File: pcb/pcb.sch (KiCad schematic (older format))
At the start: 86 parts, among them J1 USB-Mini, J2 Conn_01x04, P1 i2c-pin1, P2 i2c-pin2, SW1 SW_Push, SW10 SW_Push, SW11 SW_Push, SW12 SW_Push, SW13 SW_Push, SW14 SW_Push, SW15 SW_Push, SW16 SW_Push, SW17 SW_Push, SW18 SW_Push, SW19 SW_Push, SW2 SW_Push, SW20 SW_Push, SW21 SW_Push, SW22 SW_Push, SW23 SW_Push, SW24 SW_Push, SW25 SW_Push, SW26 SW_Push, SW27 SW_Push, SW28 SW_Push, SW29 SW_Push, SW3 SW_Push, SW30 SW_Push, SW31 SW_Push, SW32 SW_Push, SW33 SW_Push, SW34 SW_Push, SW35 SW_Push, SW36 SW_Push, SW37 SW_Push, SW38 SW_Push, SW39 SW_Push, SW4 SW_Push, SW40 SW_Push, SW5 SW_Push, SW6 SW_Push, SW7 SW_Push, SW8 SW_Push, SW9 SW_Push, U1 ProMicro, U2 TRRS

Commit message: finished case and pcb prototype
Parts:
- J2: value Conn_01x04 -> Conn_01x05; footprint Connector_PinHeader_2.54mm:PinHeader_1x04_P2.54mm_Vertical -> Connector_PinHeader_2.54mm:PinHeader_1x05_P2.54mm_Vertical; symbol Connector_Generic:Conn_01x04 -> Connector_Generic:Conn_01x05
- RSW1: footprint Keebio-Parts:SW_Tactile_SPST_Angled_MJTP1117 -> kbd:ResetSW
- U1: footprint Keebio-Parts:ArduinoProMicro-ZigZag -> Keebio-Parts:ArduinoProMicro
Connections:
- net col6: now also U1.17 (A0/PF7); no longer U1.11 (8/PB4)
- net row0: now also U1.11 (8/PB4); no longer U1.16 (15/PB1)
- net row1: now also U1.19 (A2/PF5); no longer U1.15 (14/PB3)
- net row2: now also U1.18 (A1/PF6); no longer U1.14 (16/PB2)
- net at J1.4 (ID): now also J2.5 (Pin_5)
- no-connect marks 7 -> 6
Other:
- moved on the sheet: J1
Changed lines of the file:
@@
 L keebio:USB-Mini J1
 U 1 1 60852385
-P 1700 1900
-F 0 "J1" H 1683 2597 60  0000 C CNN
-F 1 "USB-Mini" H 1683 2491 60  0000 C CNN
-F 2 "Keebio-Parts:USB-Mini-B_2leg" H 1650 1950 60  0001 C CNN
-F 3 "" H 1650 1950 60  0001 C CNN
-	1    1700 1900
+P 1150 2100
+F 0 "J1" H 1133 2797 60  0000 C CNN
+F 1 "USB-Mini" H 1133 2691 60  0000 C CNN
+F 2 "Keebio-Parts:USB-Mini-B_2leg" H 1100 2150 60  0001 C CNN
+F 3 "" H 1100 2150 60  0001 C CNN
+	1    1150 2100
 	1    0    0    -1
 $EndComp
@@
 col5
 Text HLabel 8550 5000 0    50   Input ~ 0
-col6
-Text HLabel 9950 4800 2    50   Input ~ 0
 row0
-Text HLabel 9950 4900 2    50   Input ~ 0
+Text HLabel 9950 4500 2    50   Input ~ 0
 row1
-Text HLabel 9950 5000 2    50   Input ~ 0
+Text HLabel 9950 4600 2    50   Input ~ 0
 row2
-Text HLabel 9950 5100 2    50   Input ~ 0
-row3
 Text HLabel 8550 5100 0    50   Input ~ 0
 row4
@@
 F 0 "U1" H 9250 5387 60  0000 C CNN
 F 1 "ProMicro" H 9250 5281 60  0000 C CNN
-F 2 "Keebio-Parts:ArduinoProMicro-ZigZag" V 10300 2050 60  0001 C CNN
+F 2 "Keebio-Parts:ArduinoProMicro" V 10300 2050 60  0001 C CNN
 F 3 "" V 10300 2050 60  0001 C CNN
 	1    9250 4550
@@
 F 0 "RSW1" H 9250 3405 50  0000 C CNN
 F 1 "SW_PUSH" H 9250 3314 50  0000 C CNN
-F 2 "Keebio-Parts:SW_Tactile_SPST_Angled_MJTP1117" H 9250 3313 50  0001 C CNN
+F 2 "kbd:ResetSW" H 9250 3313 50  0001 C CNN
 F 3 "" H 9250 3150 50  0000 C CNN
 	1    9250 3150
@@
 data
 $Comp
-L Connector_Generic:Conn_01x04 J2
+L Connector_Generic:Conn_01x05 J2
 U 1 1 60A9C567
-P 2900 1500
-F 0 "J2" H 2980 1492 50  0000 L CNN
-F 1 "Conn_01x04" H 2980 1401 50  0000 L CNN
-F 2 "Connector_PinHeader_2.54mm:PinHeader_1x04_P2.54mm_Vertical" H 2900 1500 50  0001 C CNN
-F 3 "~" H 2900 1500 50  0001 C CNN
-	1    2900 1500
-	1    0    0    -1
-$EndComp
-Wire Wire Line
-	2300 1850 1900 1850
-NoConn ~ 1900 1750
+P 1900 1750
+F 0 "J2" H 1980 1742 50  0000 L CNN
+F 1 "Conn_01x05" H 1980 1651 50  0000 L CNN
+F 2 "Connector_PinHeader_2.54mm:PinHeader_1x05_P2.54mm_Vertical" H 1900 1750 50  0001 C CNN
+F 3 "~" H 1900 1750 50  0001 C CNN
+	1    1900 1750
+	1    0    0    -1
+$EndComp
 NoConn ~ 8550 4000
 NoConn ~ 9950 4400
-NoConn ~ 9950 4500
-NoConn ~ 9950 4600
-NoConn ~ 9950 4700
+NoConn ~ 9950 5000
+NoConn ~ 9950 4900
 NoConn ~ 9950 4000
 $Comp
@@
 Connection ~ 6000 4400
 Wire Wire Line
-	1900 1450 2650 1450
-Wire Wire Line
-	2650 1450 2650 1500
-Wire Wire Line
-	2650 1500 2700 1500
-Wire Wire Line
-	2300 1700 2700 1700
-Wire Wire Line
-	2300 1700 2300 1850
-Wire Wire Line
-	1900 1650 2400 1650
-Wire Wire Line
-	2400 1650 2400 1600
-Wire Wire Line
-	2400 1600 2700 1600
-Wire Wire Line
-	2350 1550 2350 1400
-Wire Wire Line
-	2350 1400 2700 1400
-Wire Wire Line
-	1900 1550 2350 1550
-Wire Wire Line
 	2250 4200 2250 4050
 Wire Wire Line
@@
 	1150 6150 2250 6150
 Connection ~ 2250 6000
+Wire Wire Line
+	1350 1650 1700 1650
+Wire Wire Line
+	1700 1950 1350 1950
+Wire Wire Line
+	1350 1750 1400 1750
+Wire Wire Line
+	1400 1750 1400 1550
+Wire Wire Line
+	1400 1550 1700 1550
+Wire Wire Line
+	1350 1850 1500 1850
+Wire Wire Line
+	1500 1850 1500 1750
+Wire Wire Line
+	1500 1750 1700 1750
+Wire Wire Line
+	1350 2050 1600 2050
+Wire Wire Line
+	1600 2050 1600 1850
+Wire Wire Line
+	1600 1850 1700 1850
+Text HLabel 9950 4700 2    50   Input ~ 0
+col6
+Text HLabel 9950 5100 2    50   Input ~ 0
+row3
+NoConn ~ 9950 4800
 $EndSCHEMATC

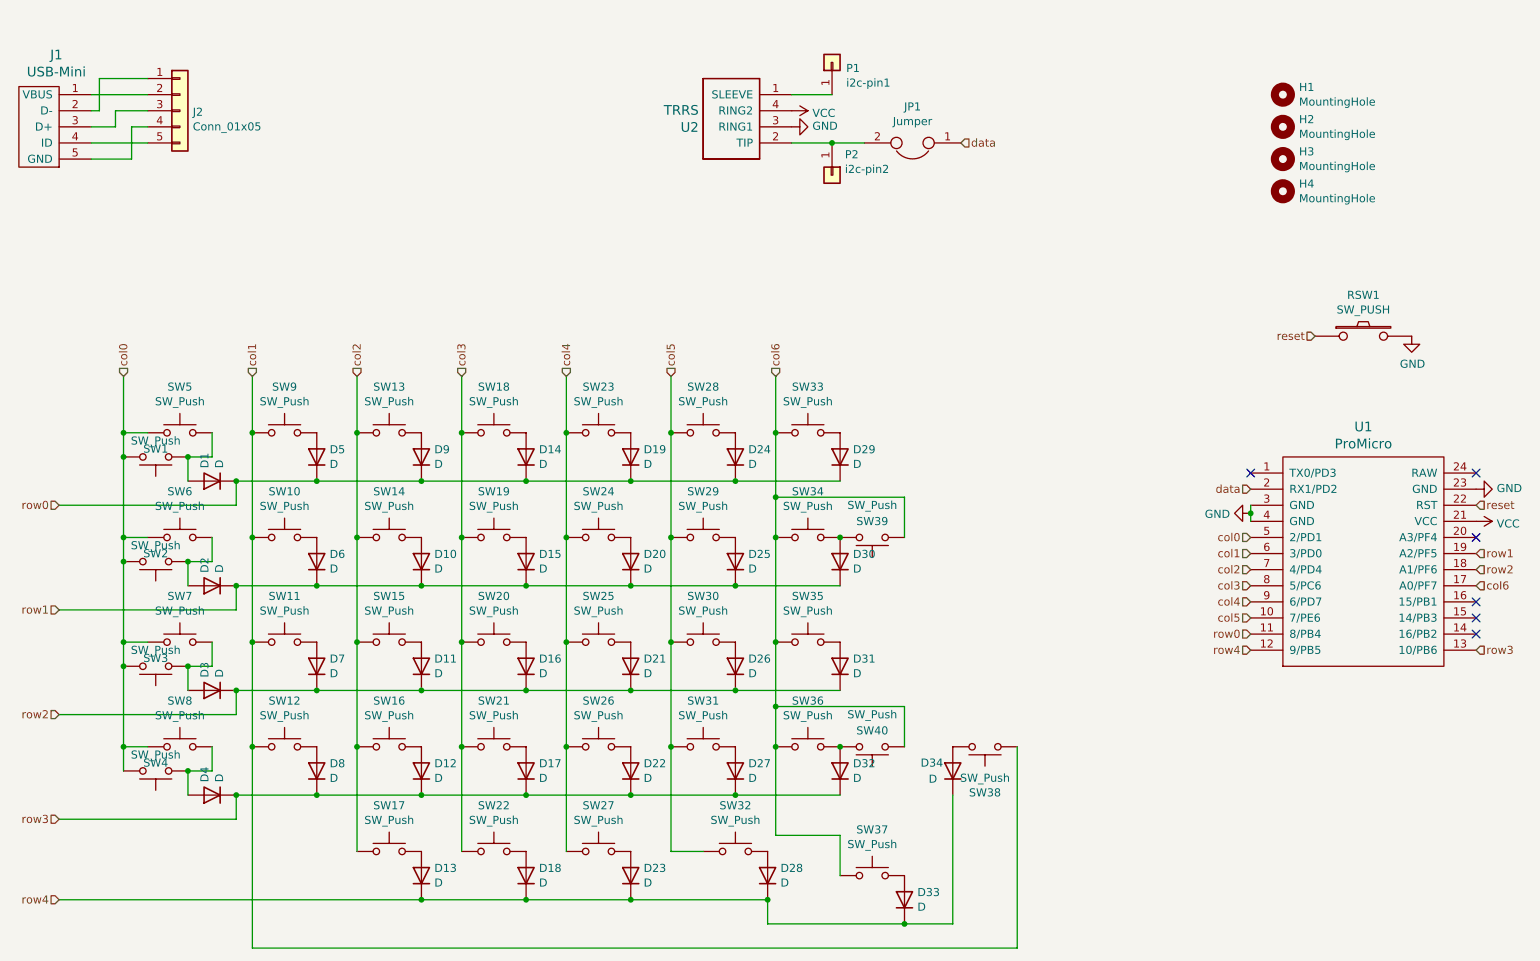
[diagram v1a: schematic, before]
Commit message: finalised pcb rev1.1
added support for an encoder
added support for a stablized 2u key on the double thumb keys
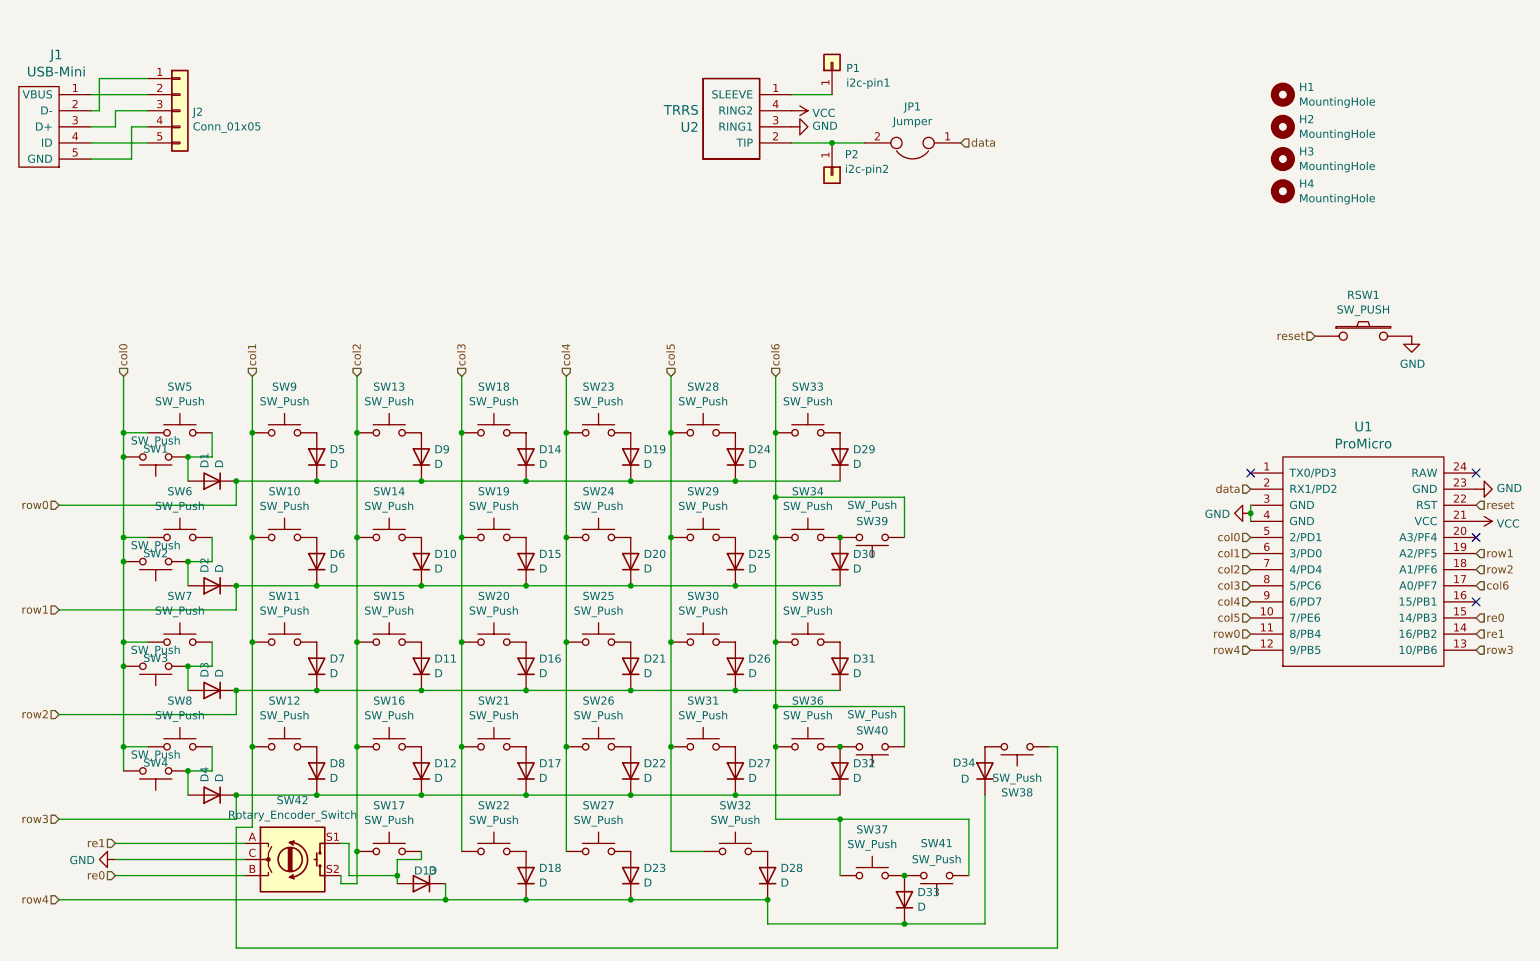
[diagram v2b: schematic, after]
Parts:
- added SW41: SW_Push, keyswitches:SW_MX_reversible, symbol Switch:SW_Push
- added SW42: Rotary_Encoder_Switch, local:RotaryEncoder_Alps_EC11E-Switch_Vertical_H20mm, symbol Device:Rotary_Encoder_Switch
- H1, H2, H3, H4: footprint local:m4.5_hole -> local:m2.4_hole_plated
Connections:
- net GND: now also SW42.C
- net col2: now also SW42.S2
- net col6: now also SW41.1
- net re1: now reaches U1.14 (16/PB2)
- net re1: now also SW42.A
- net re0: now reaches U1.15 (14/PB3)
- net re0: now also SW42.B
- net at D13.2 (A), SW17.2: now also SW42.S1
- net at D33.2 (A), SW37.2: now also SW41.2
- no-connect marks 6 -> 4
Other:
- moved on the sheet: D13, D34, SW38
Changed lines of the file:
@@
 L Device:D D13
 U 1 1 609271B4
-P 3400 6500
-F 0 "D13" V 3446 6420 50  0000 R CNN
-F 1 "D" V 3355 6420 50  0000 R CNN
-F 2 "Keebio-Parts:Diode-dual" H 3400 6500 50  0001 C CNN
-F 3 "~" H 3400 6500 50  0001 C CNN
-	1    3400 6500
-	0    -1   -1   0
+P 3400 6550
+F 0 "D13" H 3446 6470 50  0000 R CNN
+F 1 "D" H 3355 6470 50  0000 R CNN
+F 2 "Keebio-Parts:Diode-dual" H 3400 6550 50  0001 C CNN
+F 3 "~" H 3400 6550 50  0001 C CNN
+	1    3400 6550
+	-1   0    0    1
 $EndComp
 $Comp
@@
 	0    -1   -1   0
 $EndComp
-Wire Wire Line
-	3400 6650 4050 6650
 $Comp
 L Switch:SW_Push SW27
@@
 L Switch:SW_Push SW38
 U 1 1 6092E91E
-P 6900 5700
-F 0 "SW38" H 6900 5985 50  0000 C CNN
-F 1 "SW_Push" H 6900 5894 50  0000 C CNN
-F 2 "keyswitches:SW_MX_reversible" H 6900 5900 50  0001 C CNN
-F 3 "~" H 6900 5900 50  0001 C CNN
-	1    6900 5700
+P 7100 5700
+F 0 "SW38" H 7100 5985 50  0000 C CNN
+F 1 "SW_Push" H 7100 5894 50  0000 C CNN
+F 2 "keyswitches:SW_MX_reversible" H 7100 5900 50  0001 C CNN
+F 3 "~" H 7100 5900 50  0001 C CNN
+	1    7100 5700
 	-1   0    0    1
 $EndComp
@@
 L Device:D D34
 U 1 1 6092E924
-P 6700 5850
-F 0 "D34" V 6750 6050 50  0000 R CNN
-F 1 "D" V 6650 6000 50  0000 R CNN
-F 2 "Keebio-Parts:Diode-dual" H 6700 5850 50  0001 C CNN
-F 3 "~" H 6700 5850 50  0001 C CNN
-	1    6700 5850
+P 6900 5850
+F 0 "D34" V 6950 6050 50  0000 R CNN
+F 1 "D" V 6850 6000 50  0000 R CNN
+F 2 "Keebio-Parts:Diode-dual" H 6900 5850 50  0001 C CNN
+F 3 "~" H 6900 5850 50  0001 C CNN
+	1    6900 5850
 	0    -1   -1   0
 $EndComp
@@
 Connection ~ 4700 6650
 Connection ~ 4050 6650
-Connection ~ 3400 6650
 Wire Wire Line
 	5550 6650 5550 6800
@@
 Wire Wire Line
 	4950 6350 5150 6350
-Wire Wire Line
-	5600 6250 6000 6250
-Wire Wire Line
-	6000 6250 6000 6500
 $Comp
 L Device:D D5
@@
 Connection ~ 4050 4050
 Wire Wire Line
-	5600 5700 5600 6250
+	5600 5700 5600 6150
 Connection ~ 5600 5700
 Wire Wire Line
@@
 	3650 5700 3650 6350
 Connection ~ 3650 5700
-Wire Wire Line
-	3000 6350 3000 5700
 Connection ~ 3000 5700
 Wire Wire Line
-	2350 5700 2350 6950
+	2350 5700 2350 6200
 Connection ~ 2350 5700
-Wire Wire Line
-	6700 6000 6700 6800
-Wire Wire Line
-	6700 6800 6400 6800
 Connection ~ 6400 6800
-Wire Wire Line
-	7100 6950 7100 5700
-Wire Wire Line
-	2350 6950 7100 6950
 $Comp
 L Switch:SW_Push SW1
@@
 Wire Wire Line
 	1550 3400 1550 3750
-Wire Wire Line
-	1150 6650 3400 6650
 Wire Wire Line
 	1700 5050 1550 5050
@@
 NoConn ~ 8550 4000
 NoConn ~ 9950 4400
-NoConn ~ 9950 5000
-NoConn ~ 9950 4900
 NoConn ~ 9950 4000
 $Comp
@@
 F 0 "H1" H 8850 1696 50  0000 L CNN
 F 1 "MountingHole" H 8850 1605 50  0000 L CNN
-F 2 "local:m4.5_hole" H 8750 1650 50  0001 C CNN
+F 2 "local:m2.4_hole_plated" H 8750 1650 50  0001 C CNN
 F 3 "~" H 8750 1650 50  0001 C CNN
 	1    8750 1650
@@
 F 0 "H2" H 8850 1896 50  0000 L CNN
 F 1 "MountingHole" H 8850 1805 50  0000 L CNN
-F 2 "local:m4.5_hole" H 8750 1850 50  0001 C CNN
+F 2 "local:m2.4_hole_plated" H 8750 1850 50  0001 C CNN
 F 3 "~" H 8750 1850 50  0001 C CNN
 	1    8750 1850
@@
 F 0 "H3" H 8850 2096 50  0000 L CNN
 F 1 "MountingHole" H 8850 2005 50  0000 L CNN
-F 2 "local:m4.5_hole" H 8750 2050 50  0001 C CNN
+F 2 "local:m2.4_hole_plated" H 8750 2050 50  0001 C CNN
 F 3 "~" H 8750 2050 50  0001 C CNN
 	1    8750 2050
@@
 F 0 "H4" H 8850 2296 50  0000 L CNN
 F 1 "MountingHole" H 8850 2205 50  0000 L CNN
-F 2 "local:m4.5_hole" H 8750 2250 50  0001 C CNN
+F 2 "local:m2.4_hole_plated" H 8750 2250 50  0001 C CNN
 F 3 "~" H 8750 2250 50  0001 C CNN
 	1    8750 2250
@@
 row3
 NoConn ~ 9950 4800
+$Comp
+L Switch:SW_Push SW41
+U 1 1 609871D1
+P 6600 6500
+F 0 "SW41" H 6600 6300 50  0000 C CNN
+F 1 "SW_Push" H 6600 6400 50  0000 C CNN
+F 2 "keyswitches:SW_MX_reversible" H 6600 6700 50  0001 C CNN
+F 3 "~" H 6600 6700 50  0001 C CNN
+	1    6600 6500
+	-1   0    0    1
+$EndComp
+Wire Wire Line
+	7350 5700 7300 5700
+Connection ~ 6400 6500
+Wire Wire Line
+	5600 6150 6000 6150
+Wire Wire Line
+	6800 6150 6800 6500
+Connection ~ 6000 6150
+Wire Wire Line
+	6000 6150 6800 6150
+Wire Wire Line
+	6000 6150 6000 6500
+Wire Wire Line
+	6900 6800 6900 6000
+Wire Wire Line
+	6400 6800 6900 6800
+Wire Wire Line
+	7350 5700 7350 6950
+$Comp
+L Device:Rotary_Encoder_Switch SW42
+U 1 1 60A32CBC
+P 2600 6400
+F 0 "SW42" H 2600 6767 50  0000 C CNN
+F 1 "Rotary_Encoder_Switch" H 2600 6676 50  0000 C CNN
+F 2 "local:RotaryEncoder_Alps_EC11E-Switch_Vertical_H20mm" H 2450 6560 50  0001 C CNN
+F 3 "~" H 2600 6660 50  0001 C CNN
+	1    2600 6400
+	1    0    0    -1
+$EndComp
+Wire Wire Line
+	3250 6500 3250 6550
+Wire Wire Line
+	1150 6650 3550 6650
+Wire Wire Line
+	3250 6500 3250 6400
+Wire Wire Line
+	3250 6400 3400 6400
+Wire Wire Line
+	3400 6400 3400 6350
+Connection ~ 3250 6500
+Wire Wire Line
+	3550 6550 3550 6650
+Connection ~ 3550 6650
+Wire Wire Line
+	3550 6650 4050 6650
+Text HLabel 1500 6500 0    50   Input ~ 0
+re0
+Text HLabel 1500 6300 0    50   Input ~ 0
+re1
+$Comp
+L power:GND #PWR0107
+U 1 1 60A9D274
+P 1500 6400
+F 0 "#PWR0107" H 1500 6150 50  0001 C CNN
+F 1 "GND" V 1505 6272 50  0000 R CNN
+F 2 "" H 1500 6400 50  0001 C CNN
+F 3 "" H 1500 6400 50  0001 C CNN
+	1    1500 6400
+	0    1    1    0
+$EndComp
+Text HLabel 9950 4900 2    50   Input ~ 0
+re0
+Text HLabel 9950 5000 2    50   Input ~ 0
+re1
+Wire Wire Line
+	2300 6300 1500 6300
+Wire Wire Line
+	2300 6500 1500 6500
+Wire Wire Line
+	2300 6400 1500 6400
+Wire Wire Line
+	3000 5700 3000 6350
+Wire Wire Line
+	2950 6500 2950 6300
+Wire Wire Line
+	2950 6300 2900 6300
+Wire Wire Line
+	2950 6500 3250 6500
+Wire Wire Line
+	2900 6500 2900 6550
+Wire Wire Line
+	2900 6550 3000 6550
+Wire Wire Line
+	3000 6550 3000 6350
+Connection ~ 3000 6350
+Wire Wire Line
+	2350 6200 2250 6200
+Wire Wire Line
+	2250 6200 2250 6950
+Wire Wire Line
+	2250 6950 7350 6950
 $EndSCHEMATC

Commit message: updated silkscreen text
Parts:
- J2: footprint Connector_PinHeader_2.54mm:PinHeader_1x05_P2.54mm_Vertical -> local:PinHeader_1x05_P2.54mm_Vertical
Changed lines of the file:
@@
 encoding utf-8
 Sheet 1 1
-Title ""
-Date ""
-Rev ""
-Comp ""
+Title "pluckey"
+Date "2021-05-23"
+Rev "1.1"
+Comp "floookay"
 Comment1 ""
 Comment2 ""
@@
 F 0 "J2" H 1980 1742 50  0000 L CNN
 F 1 "Conn_01x05" H 1980 1651 50  0000 L CNN
-F 2 "Connector_PinHeader_2.54mm:PinHeader_1x05_P2.54mm_Vertical" H 1900 1750 50  0001 C CNN
+F 2 "local:PinHeader_1x05_P2.54mm_Vertical" H 1900 1750 50  0001 C CNN
 F 3 "~" H 1900 1750 50  0001 C CNN
 	1    1900 1750
